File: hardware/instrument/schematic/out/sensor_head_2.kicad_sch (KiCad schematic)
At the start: 3 parts, among them CN1 SM04B-SRSS-TB, U1 TMP117AIDRVR

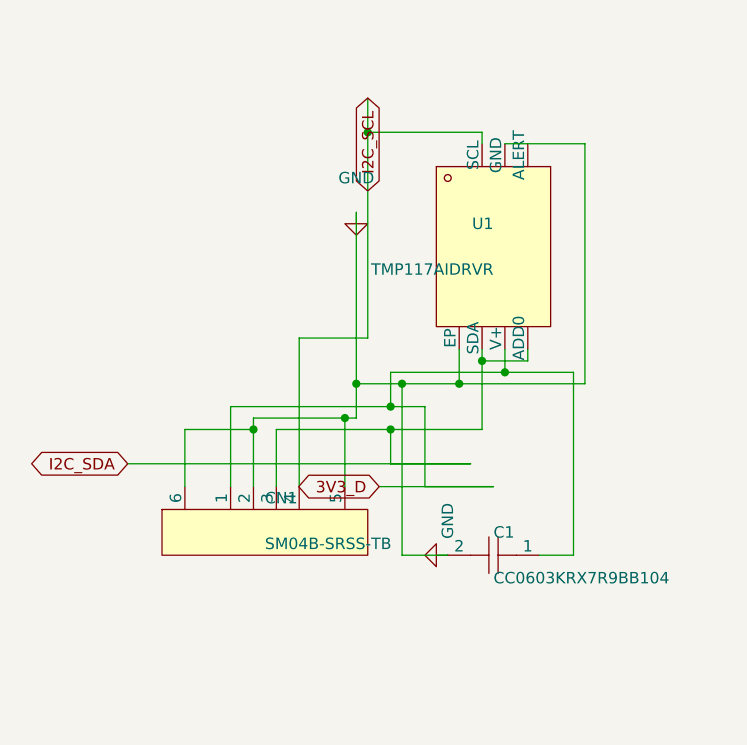
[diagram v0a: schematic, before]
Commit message: Update sensor head schematic and associated files
- Modified sensor_head_2.net to update component details, including new PWR_FLAG components (#FLG1 and #FLG2) and adjusted pin types for better clarity.
- Removed outdated sensor_head_2_kicad_erc.json file as it is no longer needed.
- Enhanced schematic_test.py to include electrical rule checks (ERC) for improved validation of circuit design.
- Introduced a new SPICE simulation file (boost.spice) for modeling the MT3608 boost converter behavior.
- Updated smoke_test.py to include checks for the boost converter's performance and safety metrics.
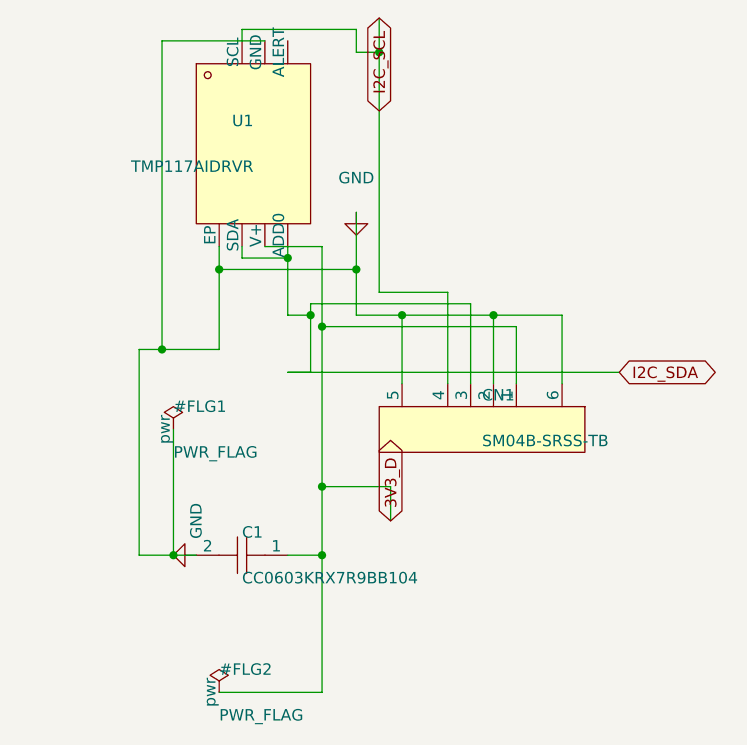
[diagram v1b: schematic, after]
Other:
- moved on the sheet: C1, CN1, U1
